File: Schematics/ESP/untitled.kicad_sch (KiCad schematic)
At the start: 7 parts, among them J1 Conn_01x04_Male, J10 Conn_01x03_Socket, J2 Conn_01x04_Male, J9 Conn_01x03_Socket, U1 NUCLEO64-F411RE

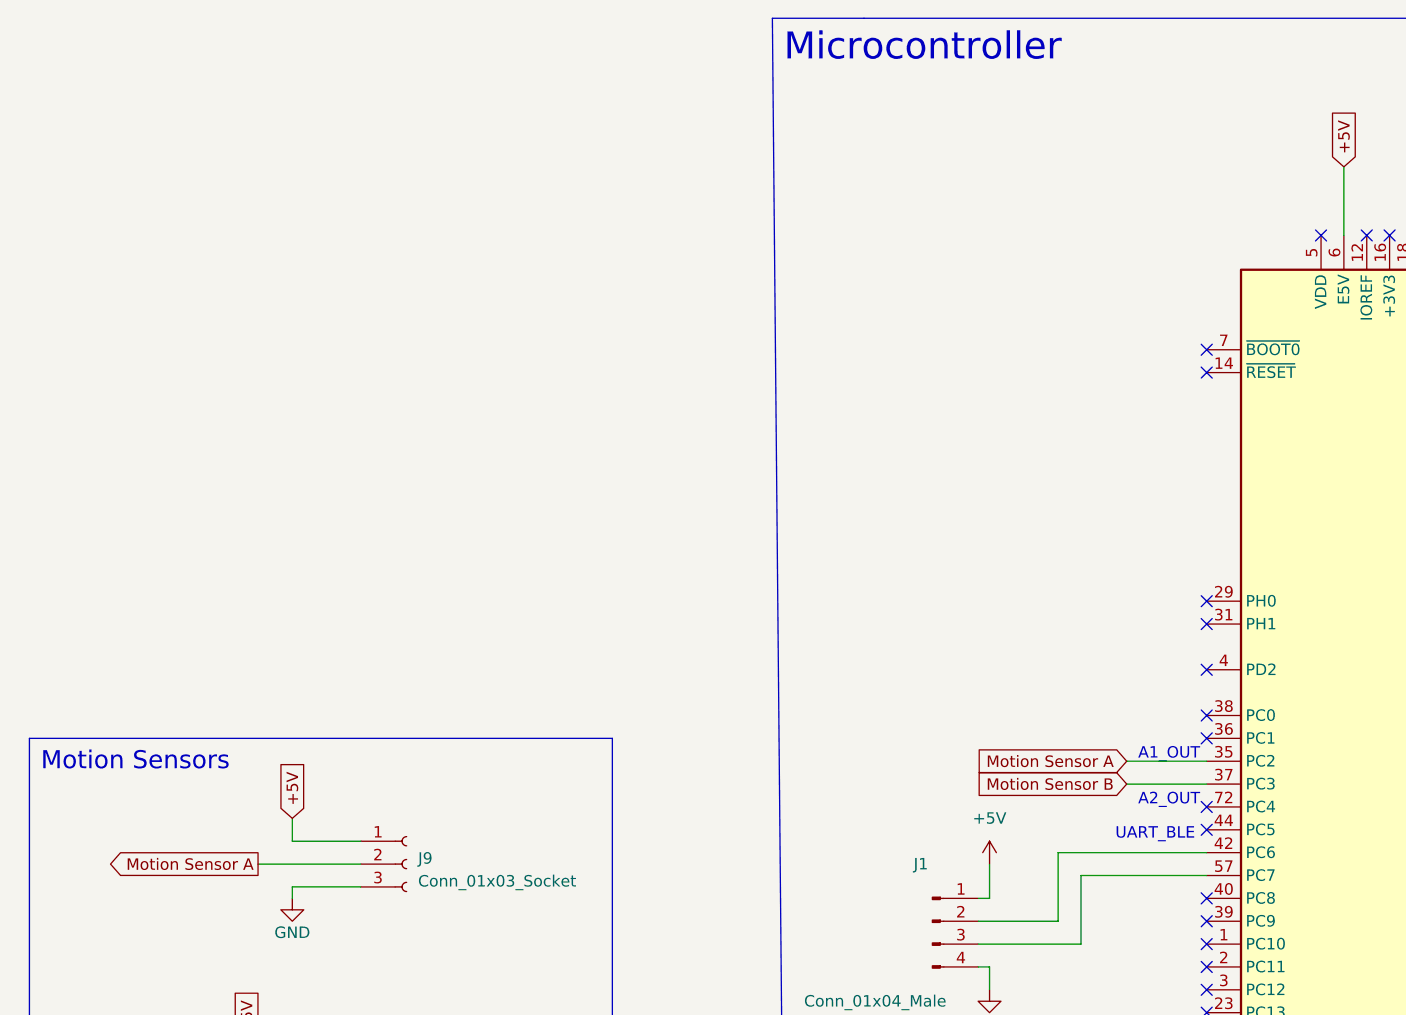
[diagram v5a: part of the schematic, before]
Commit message: Added bumpers
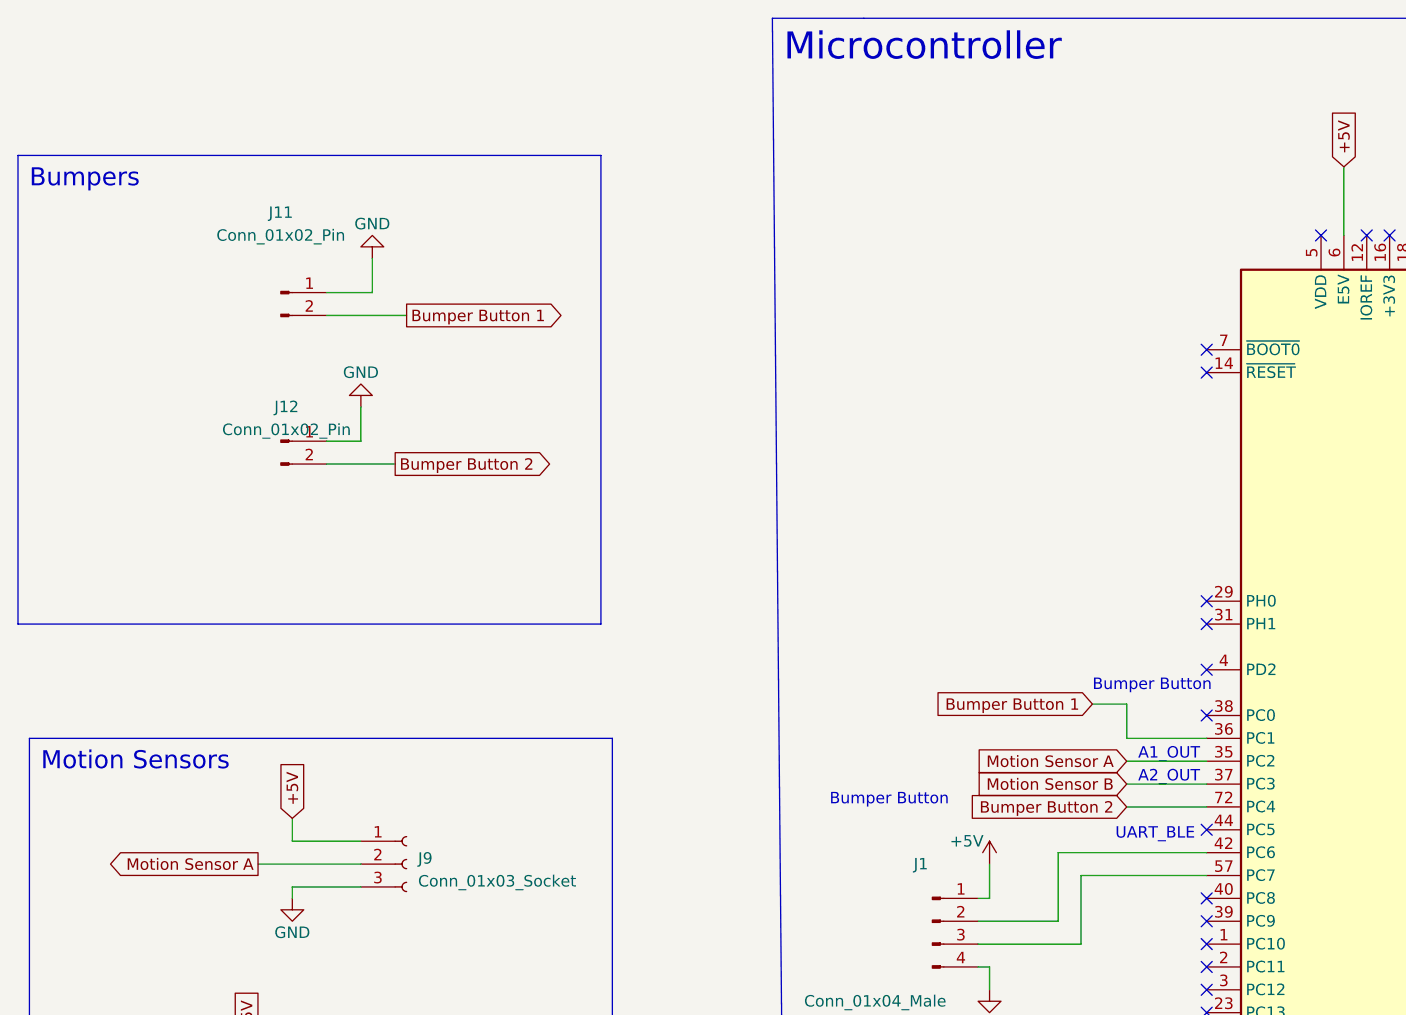
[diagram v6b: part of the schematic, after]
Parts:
- added J11, J12: Conn_01x02_Pin, Connector_PinSocket_1.00mm:PinSocket_1x02_P1.00mm_Vertical, symbol Connector:Conn_01x02_Pin
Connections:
- net GND: now also J11.1 (Pin_1), J12.1 (Pin_1)
- net Bumper Button 1: now reaches U1.36 (PC1)
- net Bumper Button 1: now also J11.2 (Pin_2)
- net Bumper Button 2: now reaches U1.72 (PC4)
- net Bumper Button 2: now also J12.2 (Pin_2)
- no-connect marks 51 -> 49
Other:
- note added: "Bumper Button"
- note added: "Bumpers"
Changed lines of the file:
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@@
   (no_connect (at 156.21 87.63))
   (no_connect (at 156.21 123.19))
-  (no_connect (at 156.21 107.95))
   (no_connect (at 212.09 57.15))
   (no_connect (at 156.21 59.69))
@@
   (no_connect (at 156.21 135.89))
   (no_connect (at 212.09 82.55))
-  (no_connect (at 156.21 100.33))
   (wire (pts (xy 132.08 125.73) (xy 132.08 128.27))
     (stroke (width 0) (type default))
@@
     (stroke (width 0) (type default))
   )
+  (wire (pts (xy 147.32 100.33) (xy 147.32 96.52))
+    (stroke (width 0) (type default))
+  )
   (wire (pts (xy 49.53 137.16) (xy 57.15 137.16))
     (stroke (width 0) (type default))
@@
     (stroke (width 0) (type default))
   )
+  (wire (pts (xy 58.42 50.8) (xy 63.5 50.8))
+    (stroke (width 0) (type default))
+  )
   (wire (pts (xy 168.91 146.05) (xy 168.91 147.32))
     (stroke (width 0) (type default))
@@
     (stroke (width 0) (type default))
   )
+  (wire (pts (xy 63.5 50.8) (xy 63.5 46.99))
+    (stroke (width 0) (type default))
+  )
   (wire (pts (xy 54.61 116.84) (xy 54.61 118.11))
     (stroke (width 0) (type default))
@@
     (stroke (width 0) (type default))
   )
+  (wire (pts (xy 156.21 100.33) (xy 147.32 100.33))
+    (stroke (width 0) (type default))
+  )
   (wire (pts (xy 49.53 142.24) (xy 49.53 143.51))
     (stroke (width 0) (type default))
@@
     (stroke (width 0) (type default))
   )
+  (wire (pts (xy 62.23 67.31) (xy 62.23 63.5))
+    (stroke (width 0) (type default))
+  )
   (wire (pts (xy 189.23 147.32) (xy 191.77 147.32))
     (stroke (width 0) (type default))
@@
     (stroke (width 0) (type default))
   )
+  (wire (pts (xy 143.51 96.52) (xy 147.32 96.52))
+    (stroke (width 0) (type default))
+  )
+  (wire (pts (xy 147.32 107.95) (xy 156.21 107.95))
+    (stroke (width 0) (type default))
+  )
   (wire (pts (xy 212.09 59.69) (xy 224.79 59.69))
     (stroke (width 0) (type default))
@@
     (stroke (width 0) (type default))
   )
+  (wire (pts (xy 58.42 67.31) (xy 62.23 67.31))
+    (stroke (width 0) (type default))
+  )
   (wire (pts (xy 251.46 133.35) (xy 251.46 124.46))
     (stroke (width 0) (type default))
@@
     (stroke (width 0) (type default))
   )
+  (wire (pts (xy 58.42 53.34) (xy 67.31 53.34))
+    (stroke (width 0) (type default))
+  )
   (wire (pts (xy 179.07 147.32) (xy 179.07 146.05))
     (stroke (width 0) (type default))
@@
     (stroke (width 0) (type default))
   )
+  (wire (pts (xy 58.42 69.85) (xy 66.04 69.85))
+    (stroke (width 0) (type default))
+  )
   (wire (pts (xy 139.7 113.03) (xy 139.7 120.65))
     (stroke (width 0) (type default))
@@
     (stroke (width 0) (type default))
   )
+  (rectangle (start 24.13 35.56) (end 88.9 87.63)
+    (stroke (width 0) (type default))
+    (fill (type none))
+  )
   (rectangle (start 25.4 100.33) (end 90.17 152.4)
     (stroke (width 0) (type default))
     (fill (type none))
   )
+  (text "Bumpers" (at 25.4 39.37 0)
+    (effects (font (size 2 2)) (justify left bottom))
+  )
   (text "\n2 PMW for motor drivers" (at 220.98 78.74 0)
+    (effects (font (size 1.27 1.27)) (justify left bottom))
+  )
+  (text "Bumper Button" (at 143.51 95.25 0)
     (effects (font (size 1.27 1.27)) (justify left bottom))
   )
@@
     (effects (font (size 3 3)) (justify left bottom))
   )
-  (text "A2_OUT" (at 148.59 107.95 0)
+  (text "A2_OUT" (at 148.59 105.41 0)
     (effects (font (size 1.27 1.27)) (justify left bottom))
   )
@@
     (effects (font (size 1.27 1.27)) (justify left bottom))
   )
+  (text "Bumper Button" (at 114.3 107.95 0)
+    (effects (font (size 1.27 1.27)) (justify left bottom))
+  )
   (text "UART_BLE" (at 146.05 111.76 0)
     (effects (font (size 1.27 1.27)) (justify left bottom))
@@
   (text "I2C2_SDA" (at 213.36 123.19 0)
     (effects (font (size 1.27 1.27)) (justify left bottom))
+  )
+  (global_label "Bumper Button 1" (shape output) (at 67.31 53.34 0) (fields_autoplaced)
+    (effects (font (size 1.27 1.27)) (justify left))
+    (property "Intersheetrefs" "${INTERSHEET_REFS}" (at 86.2538 53.34 0)
+      (effects (font (size 1.27 1.27)) (justify left) hide)
+    )
   )
   (global_label "Fan Signal" (shape output) (at 220.98 115.57 0) (fields_autoplaced)
@@
     )
   )
+  (global_label "Bumper Button 1" (shape input) (at 143.51 96.52 180) (fields_autoplaced)
+    (effects (font (size 1.27 1.27)) (justify right))
+    (property "Intersheetrefs" "${INTERSHEET_REFS}" (at 124.5662 96.52 0)
+      (effects (font (size 1.27 1.27)) (justify right) hide)
+    )
+  )
   (global_label "+5V" (shape input) (at 54.61 109.22 90) (fields_autoplaced)
     (effects (font (size 1.27 1.27)) (justify left))
@@
     )
   )
+  (global_label "Bumper Button 2" (shape output) (at 66.04 69.85 0) (fields_autoplaced)
+    (effects (font (size 1.27 1.27)) (justify left))
+    (property "Intersheetrefs" "${INTERSHEET_REFS}" (at 84.9838 69.85 0)
+      (effects (font (size 1.27 1.27)) (justify left) hide)
+    )
+  )
+  (global_label "Bumper Button 2" (shape input) (at 147.32 107.95 180) (fields_autoplaced)
+    (effects (font (size 1.27 1.27)) (justify right))
+    (property "Intersheetrefs" "${INTERSHEET_REFS}" (at 128.3762 107.95 0)
+      (effects (font (size 1.27 1.27)) (justify right) hide)
+    )
+  )
   (global_label "Battery level" (shape input) (at 224.79 59.69 0) (fields_autoplaced)
     (effects (font (size 1.27 1.27)) (justify left))
@@
     )
   )
+  (symbol (lib_id "Connector:Conn_01x02_Pin") (at 53.34 67.31 0) (unit 1)
+    (in_bom yes) (on_board yes) (dnp no) (fields_autoplaced)
+    (property "Reference" "J12" (at 53.975 63.5 0)
+      (effects (font (size 1.27 1.27)))
+    )
+    (property "Value" "Conn_01x02_Pin" (at 53.975 66.04 0)
+      (effects (font (size 1.27 1.27)))
+    )
+    (property "Footprint" "Connector_PinSocket_1.00mm:PinSocket_1x02_P1.00mm_Vertical" (at 53.34 67.31 0)
+      (effects (font (size 1.27 1.27)) hide)
+    )
+    (property "Datasheet" "~" (at 53.34 67.31 0)
+      (effects (font (size 1.27 1.27)) hide)
+    )
+    (pin "1")
+    (pin "2")
+    (instances
+      (project "ESP"
+        (path "/b616d203-cf5c-462f-b907-860a8573592a/d73e0648-2dfb-47f8-9e43-38f378a4f4ca"
+          (reference "J12") (unit 1)
+        )
+      )
+    )
+  )
   (symbol (lib_id "power:+5V") (at 132.08 114.3 0) (unit 1)
     (in_bom yes) (on_board yes) (dnp no)
@@
       (effects (font (size 1.27 1.27)) hide)
     )
-    (property "Value" "+5V" (at 132.08 109.22 0)
+    (property "Value" "+5V" (at 129.54 111.76 0)
       (effects (font (size 1.27 1.27)))
     )
@@
         (path "/b616d203-cf5c-462f-b907-860a8573592a/d73e0648-2dfb-47f8-9e43-38f378a4f4ca"
           (reference "R7") (unit 1)
+        )
+      )
+    )
+  )
+  (symbol (lib_id "power:GND") (at 62.23 63.5 180) (unit 1)
+    (in_bom yes) (on_board yes) (dnp no) (fields_autoplaced)
+    (property "Reference" "#PWR?" (at 62.23 57.15 0)
+      (effects (font (size 1.27 1.27)) hide)
+    )
+    (property "Value" "GND" (at 62.23 59.69 0)
+      (effects (font (size 1.27 1.27)))
+    )
+    (property "Footprint" "" (at 62.23 63.5 0)
+      (effects (font (size 1.27 1.27)) hide)
+    )
+    (property "Datasheet" "" (at 62.23 63.5 0)
+      (effects (font (size 1.27 1.27)) hide)
+    )
+    (pin "1")
+    (instances
+      (project "ESP"
+        (path "/b616d203-cf5c-462f-b907-860a8573592a"
+          (reference "#PWR?") (unit 1)
+        )
+        (path "/b616d203-cf5c-462f-b907-860a8573592a/d73e0648-2dfb-47f8-9e43-38f378a4f4ca"
+          (reference "#PWR030") (unit 1)
         )
       )
@@
     )
   )
+  (symbol (lib_id "power:GND") (at 63.5 46.99 180) (unit 1)
+    (in_bom yes) (on_board yes) (dnp no) (fields_autoplaced)
+    (property "Reference" "#PWR?" (at 63.5 40.64 0)
+      (effects (font (size 1.27 1.27)) hide)
+    )
+    (property "Value" "GND" (at 63.5 43.18 0)
+      (effects (font (size 1.27 1.27)))
+    )
+    (property "Footprint" "" (at 63.5 46.99 0)
+      (effects (font (size 1.27 1.27)) hide)
+    )
+    (property "Datasheet" "" (at 63.5 46.99 0)
+      (effects (font (size 1.27 1.27)) hide)
+    )
+    (pin "1")
+    (instances
+      (project "ESP"
+        (path "/b616d203-cf5c-462f-b907-860a8573592a"
+          (reference "#PWR?") (unit 1)
+        )
+        (path "/b616d203-cf5c-462f-b907-860a8573592a/d73e0648-2dfb-47f8-9e43-38f378a4f4ca"
+          (reference "#PWR031") (unit 1)
+        )
+      )
+    )
+  )
   (symbol (lib_id "power:GND") (at 168.91 149.86 0) (unit 1)
     (in_bom yes) (on_board yes) (dnp no) (fields_autoplaced)
@@
         )
       )
+    )
+  )
+  (symbol (lib_id "Connector:Conn_01x02_Pin") (at 53.34 50.8 0) (unit 1)
+    (in_bom yes) (on_board yes) (dnp no)
+    (property "Reference" "J11" (at 53.34 41.91 0)
+      (effects (font (size 1.27 1.27)))
+    )
+    (property "Value" "Conn_01x02_Pin" (at 53.34 44.45 0)
+      (effects (font (size 1.27 1.27)))
+    )
+    (property "Footprint" "Connector_PinSocket_1.00mm:PinSocket_1x02_P1.00mm_Vertical" (at 53.34 50.8 0)
+      (effects (font (size 1.27 1.27)) hide)
+    )
+    (property "Datasheet" "~" (at 53.34 50.8 0)
+      (effects (font (size 1.27 1.27)) hide)
+    )
+    (pin "1")
+    (pin "2")
+    (instances
+      (project "ESP"
+        (path "/b616d203-cf5c-462f-b907-860a8573592a/d73e0648-2dfb-47f8-9e43-38f378a4f4ca"
+          (reference "J11") (unit 1)
+        )
+      )

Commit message: Can Pull
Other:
- note added: "Nucleo Board Sheet"
- moved on the sheet: J11, J12
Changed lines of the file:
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@@
     (stroke (width 0) (type default))
   )
-  (wire (pts (xy 58.42 50.8) (xy 63.5 50.8))
+  (wire (pts (xy 59.69 60.96) (xy 64.77 60.96))
     (stroke (width 0) (type default))
   )
@@
     (stroke (width 0) (type default))
   )
-  (wire (pts (xy 63.5 50.8) (xy 63.5 46.99))
+  (wire (pts (xy 64.77 60.96) (xy 64.77 57.15))
     (stroke (width 0) (type default))
   )
@@
     (stroke (width 0) (type default))
   )
-  (wire (pts (xy 62.23 67.31) (xy 62.23 63.5))
+  (wire (pts (xy 63.5 77.47) (xy 63.5 73.66))
     (stroke (width 0) (type default))
   )
@@
     (stroke (width 0) (type default))
   )
-  (wire (pts (xy 58.42 67.31) (xy 62.23 67.31))
+  (wire (pts (xy 59.69 77.47) (xy 63.5 77.47))
     (stroke (width 0) (type default))
   )
@@
     (stroke (width 0) (type default))
   )
-  (wire (pts (xy 58.42 53.34) (xy 67.31 53.34))
+  (wire (pts (xy 59.69 63.5) (xy 68.58 63.5))
     (stroke (width 0) (type default))
   )
@@
     (stroke (width 0) (type default))
   )
-  (wire (pts (xy 58.42 69.85) (xy 66.04 69.85))
+  (wire (pts (xy 59.69 80.01) (xy 67.31 80.01))
     (stroke (width 0) (type default))
   )
@@
     (stroke (width 0) (type default))
   )
-  (rectangle (start 24.13 35.56) (end 88.9 87.63)
+  (rectangle (start 25.4 45.72) (end 90.17 97.79)
     (stroke (width 0) (type default))
     (fill (type none))
@@
     (fill (type none))
   )
-  (text "Bumpers" (at 25.4 39.37 0)
+  (text "Bumpers" (at 26.67 49.53 0)
     (effects (font (size 2 2)) (justify left bottom))
+  )
+  (text "Nucleo Board Sheet" (at 16.51 21.59 0)
+    (effects (font (size 4 4) bold) (justify left bottom))
   )
   (text "\n2 PMW for motor drivers" (at 220.98 78.74 0)
@@
     (effects (font (size 1.27 1.27)) (justify left bottom))
   )
-  (global_label "Bumper Button 1" (shape output) (at 67.31 53.34 0) (fields_autoplaced)
+  (global_label "Bumper Button 1" (shape output) (at 68.58 63.5 0) (fields_autoplaced)
     (effects (font (size 1.27 1.27)) (justify left))
-    (property "Intersheetrefs" "${INTERSHEET_REFS}" (at 86.2538 53.34 0)
+    (property "Intersheetrefs" "${INTERSHEET_REFS}" (at 87.5238 63.5 0)
       (effects (font (size 1.27 1.27)) (justify left) hide)
     )
@@
     )
   )
-  (global_label "Bumper Button 2" (shape output) (at 66.04 69.85 0) (fields_autoplaced)
+  (global_label "Bumper Button 2" (shape output) (at 67.31 80.01 0) (fields_autoplaced)
     (effects (font (size 1.27 1.27)) (justify left))
-    (property "Intersheetrefs" "${INTERSHEET_REFS}" (at 84.9838 69.85 0)
+    (property "Intersheetrefs" "${INTERSHEET_REFS}" (at 86.2538 80.01 0)
       (effects (font (size 1.27 1.27)) (justify left) hide)
     )
@@
     )
   )
-  (symbol (lib_id "Connector:Conn_01x02_Pin") (at 53.34 67.31 0) (unit 1)
-    (in_bom yes) (on_board yes) (dnp no) (fields_autoplaced)
-    (property "Reference" "J12" (at 53.975 63.5 0)
-      (effects (font (size 1.27 1.27)))
-    )
-    (property "Value" "Conn_01x02_Pin" (at 53.975 66.04 0)
-      (effects (font (size 1.27 1.27)))
-    )
-    (property "Footprint" "Connector_PinSocket_1.00mm:PinSocket_1x02_P1.00mm_Vertical" (at 53.34 67.31 0)
-      (effects (font (size 1.27 1.27)) hide)
-    )
-    (property "Datasheet" "~" (at 53.34 67.31 0)
+  (symbol (lib_id "Connector:Conn_01x02_Pin") (at 54.61 77.47 0) (unit 1)
+    (in_bom yes) (on_board yes) (dnp no) (fields_autoplaced)
+    (property "Reference" "J12" (at 55.245 73.66 0)
+      (effects (font (size 1.27 1.27)))
+    )
+    (property "Value" "Conn_01x02_Pin" (at 55.245 76.2 0)
+      (effects (font (size 1.27 1.27)))
+    )
+    (property "Footprint" "Connector_PinSocket_1.00mm:PinSocket_1x02_P1.00mm_Vertical" (at 54.61 77.47 0)
+      (effects (font (size 1.27 1.27)) hide)
+    )
+    (property "Datasheet" "~" (at 54.61 77.47 0)
       (effects (font (size 1.27 1.27)) hide)
     )
@@
     )
   )
-  (symbol (lib_id "power:GND") (at 62.23 63.5 180) (unit 1)
-    (in_bom yes) (on_board yes) (dnp no) (fields_autoplaced)
-    (property "Reference" "#PWR?" (at 62.23 57.15 0)
-      (effects (font (size 1.27 1.27)) hide)
-    )
-    (property "Value" "GND" (at 62.23 59.69 0)
-      (effects (font (size 1.27 1.27)))
-    )
-    (property "Footprint" "" (at 62.23 63.5 0)
-      (effects (font (size 1.27 1.27)) hide)
-    )
-    (property "Datasheet" "" (at 62.23 63.5 0)
+  (symbol (lib_id "power:GND") (at 63.5 73.66 180) (unit 1)
+    (in_bom yes) (on_board yes) (dnp no) (fields_autoplaced)
+    (property "Reference" "#PWR?" (at 63.5 67.31 0)
+      (effects (font (size 1.27 1.27)) hide)
+    )
+    (property "Value" "GND" (at 63.5 69.85 0)
+      (effects (font (size 1.27 1.27)))
+    )
+    (property "Footprint" "" (at 63.5 73.66 0)
+      (effects (font (size 1.27 1.27)) hide)
+    )
+    (property "Datasheet" "" (at 63.5 73.66 0)
       (effects (font (size 1.27 1.27)) hide)
     )
@@
     )
   )
-  (symbol (lib_id "power:GND") (at 63.5 46.99 180) (unit 1)
-    (in_bom yes) (on_board yes) (dnp no) (fields_autoplaced)
-    (property "Reference" "#PWR?" (at 63.5 40.64 0)
-      (effects (font (size 1.27 1.27)) hide)
-    )
-    (property "Value" "GND" (at 63.5 43.18 0)
-      (effects (font (size 1.27 1.27)))
-    )
-    (property "Footprint" "" (at 63.5 46.99 0)
-      (effects (font (size 1.27 1.27)) hide)
-    )
-    (property "Datasheet" "" (at 63.5 46.99 0)
+  (symbol (lib_id "power:GND") (at 64.77 57.15 180) (unit 1)
+    (in_bom yes) (on_board yes) (dnp no) (fields_autoplaced)
+    (property "Reference" "#PWR?" (at 64.77 50.8 0)
+      (effects (font (size 1.27 1.27)) hide)
+    )
+    (property "Value" "GND" (at 64.77 53.34 0)
+      (effects (font (size 1.27 1.27)))
+    )
+    (property "Footprint" "" (at 64.77 57.15 0)
+      (effects (font (size 1.27 1.27)) hide)
+    )
+    (property "Datasheet" "" (at 64.77 57.15 0)
       (effects (font (size 1.27 1.27)) hide)
     )
@@
     )
   )
-  (symbol (lib_id "Connector:Conn_01x02_Pin") (at 53.34 50.8 0) (unit 1)
+  (symbol (lib_id "Connector:Conn_01x02_Pin") (at 54.61 60.96 0) (unit 1)
     (in_bom yes) (on_board yes) (dnp no)
-    (property "Reference" "J11" (at 53.34 41.91 0)
-      (effects (font (size 1.27 1.27)))
-    )
-    (property "Value" "Conn_01x02_Pin" (at 53.34 44.45 0)
-      (effects (font (size 1.27 1.27)))
-    )
-    (property "Footprint" "Connector_PinSocket_1.00mm:PinSocket_1x02_P1.00mm_Vertical" (at 53.34 50.8 0)
-      (effects (font (size 1.27 1.27)) hide)
-    )
-    (property "Datasheet" "~" (at 53.34 50.8 0)
-      (effects (font (size 1.27 1.27)) hide)
-    )
+    (property "Reference" "J11" (at 54.61 52.07 0)
+      (effects (font (size 1.27 1.27)))
+    )
+    (property "Value" "Conn_01x02_Pin" (at 54.61 54.61 0)
+      (effects (font (size 1.27 1.27)))
+    )
+    (property "Footprint" "Connector_PinSocket_1.00mm:PinSocket_1x02_P1.00mm_Vertical" (at 54.61 60.96 0)
+      (effects (font (size 1.27 1.27)) hide)
+    )
+    (property "Datasheet" "~" (at 54.61 60.96 0)
+      (effects (font (size 1.27 1.27)) hide)
+    )
